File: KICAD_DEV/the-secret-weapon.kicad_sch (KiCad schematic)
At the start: 10 parts, among them J1 USB_C_Receptacle_USB2.0_14P, U1 STM32H757IITx, U2 TPS26750, U3 TPD4S480

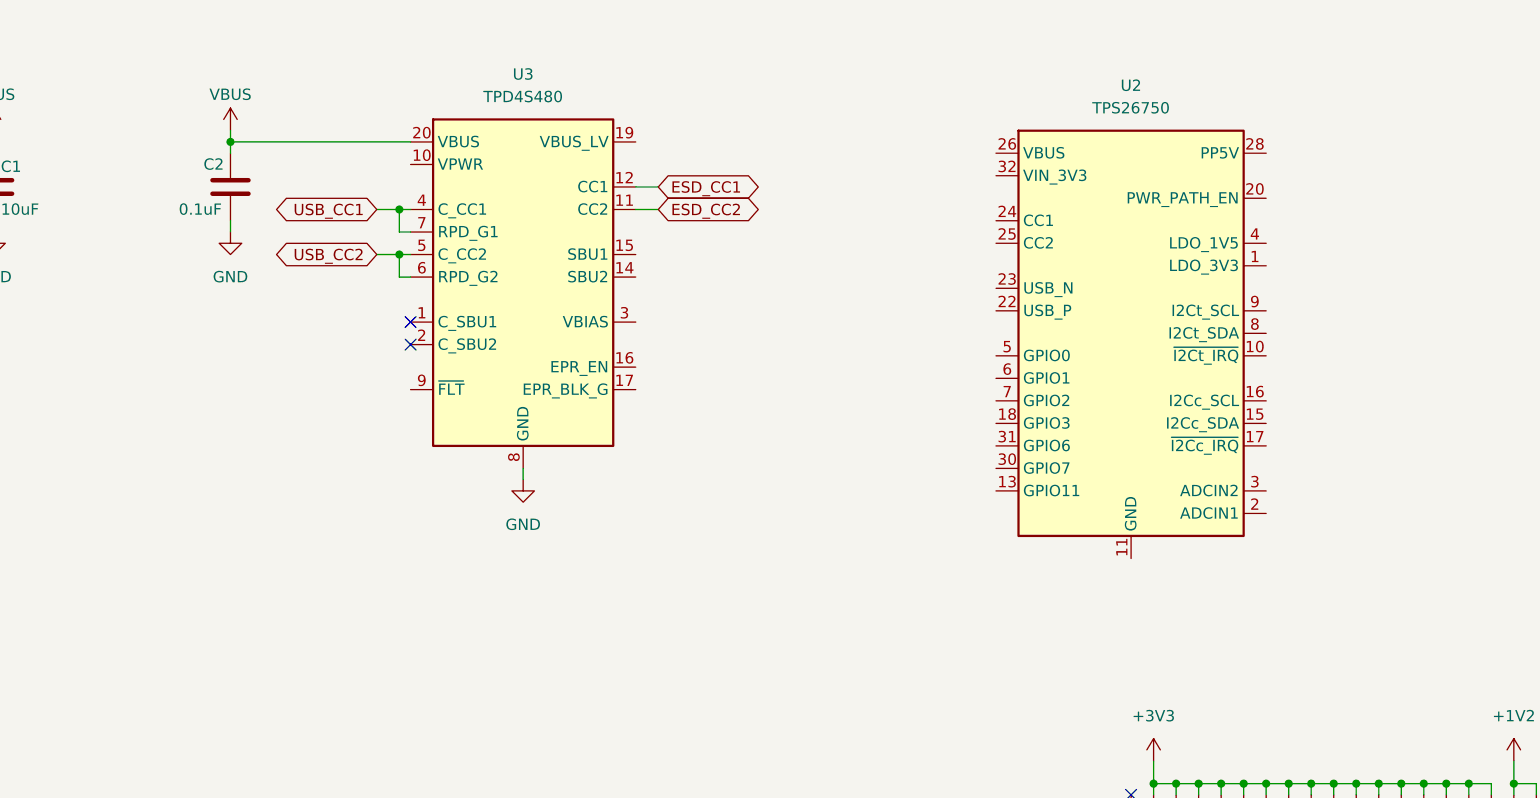
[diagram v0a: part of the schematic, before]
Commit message: finished wiring USB ESD protection
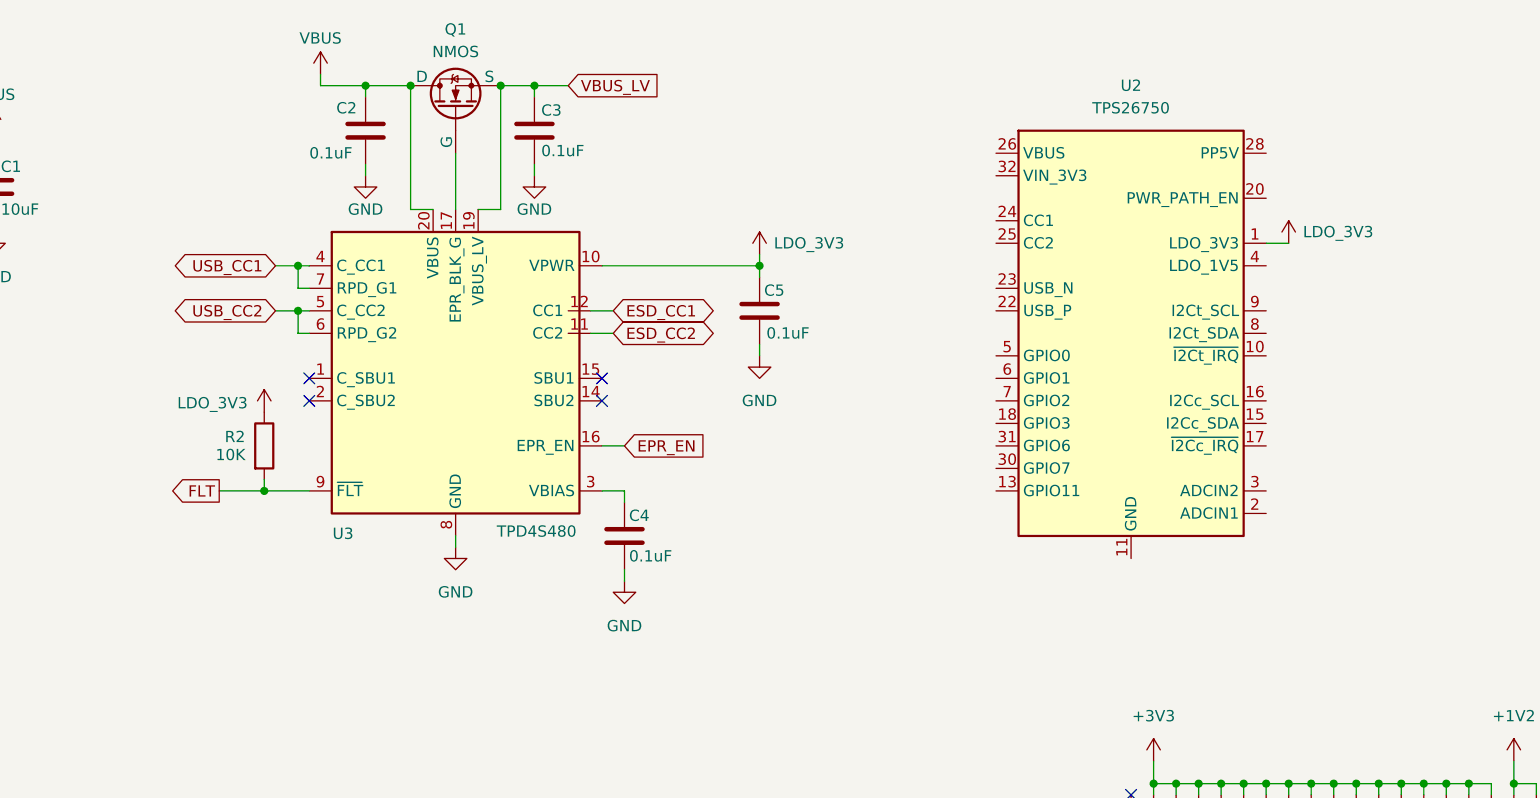
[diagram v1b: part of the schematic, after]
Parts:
- added C3, C4, C5: 0.1uF, symbol Device:C
- added Q1: NMOS, symbol Simulation_SPICE:NMOS
- added R2: 10K, symbol Device:R
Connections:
- net GND: now also C3.2, C4.2, C5.2; no longer U3.13 (GND), U3.16 (EPR_EN), U3.17 (EPR_BLK_G), U3.18 (GND), U3.21 (GND)
- net VBUS: now also Q1.1 (D)
- net LDO_3V3: now reaches U2.1 (LDO_3V3)
- net LDO_3V3: now also U3.10 (VPWR), C5.1, R2.1
- net EPR_EN: now reaches U3.16 (EPR_EN)
- net at U3.17 (EPR_BLK_G): now also Q1.2 (G)
- net VBUS_LV: now reaches U3.19 (VBUS_LV)
- net VBUS_LV: now also C3.1, Q1.3 (S)
- net at U3.3 (VBIAS): now also C4.1
- net FLT: now reaches U3.9 (~{FLT})
- net FLT: now also R2.2
- new net: U3.13 (GND), U3.16 (EPR_EN)
- new net: U3.17 (EPR_BLK_G), U3.18 (GND), U3.21 (GND)
- no-connect marks 3 -> 5
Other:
- moved on the sheet: U3

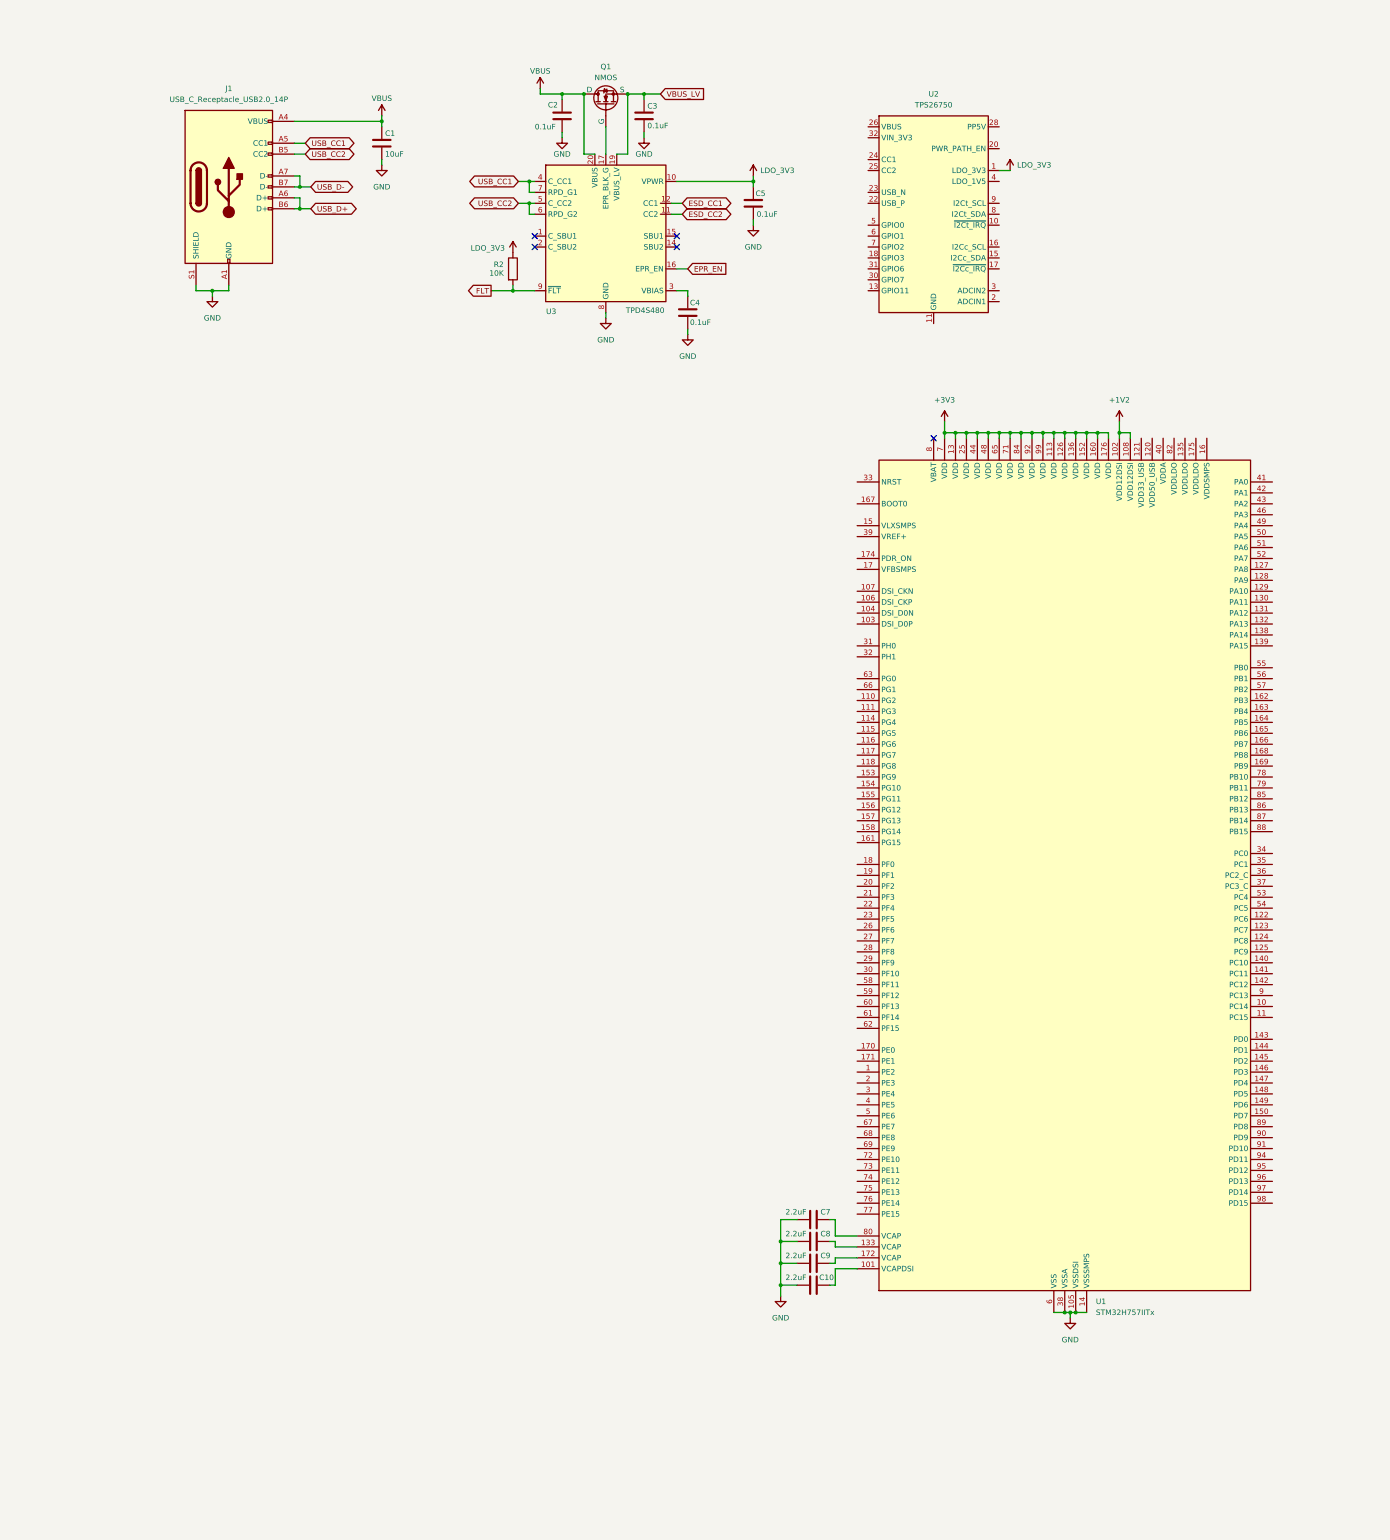
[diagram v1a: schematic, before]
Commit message: starting to wire my USB PD
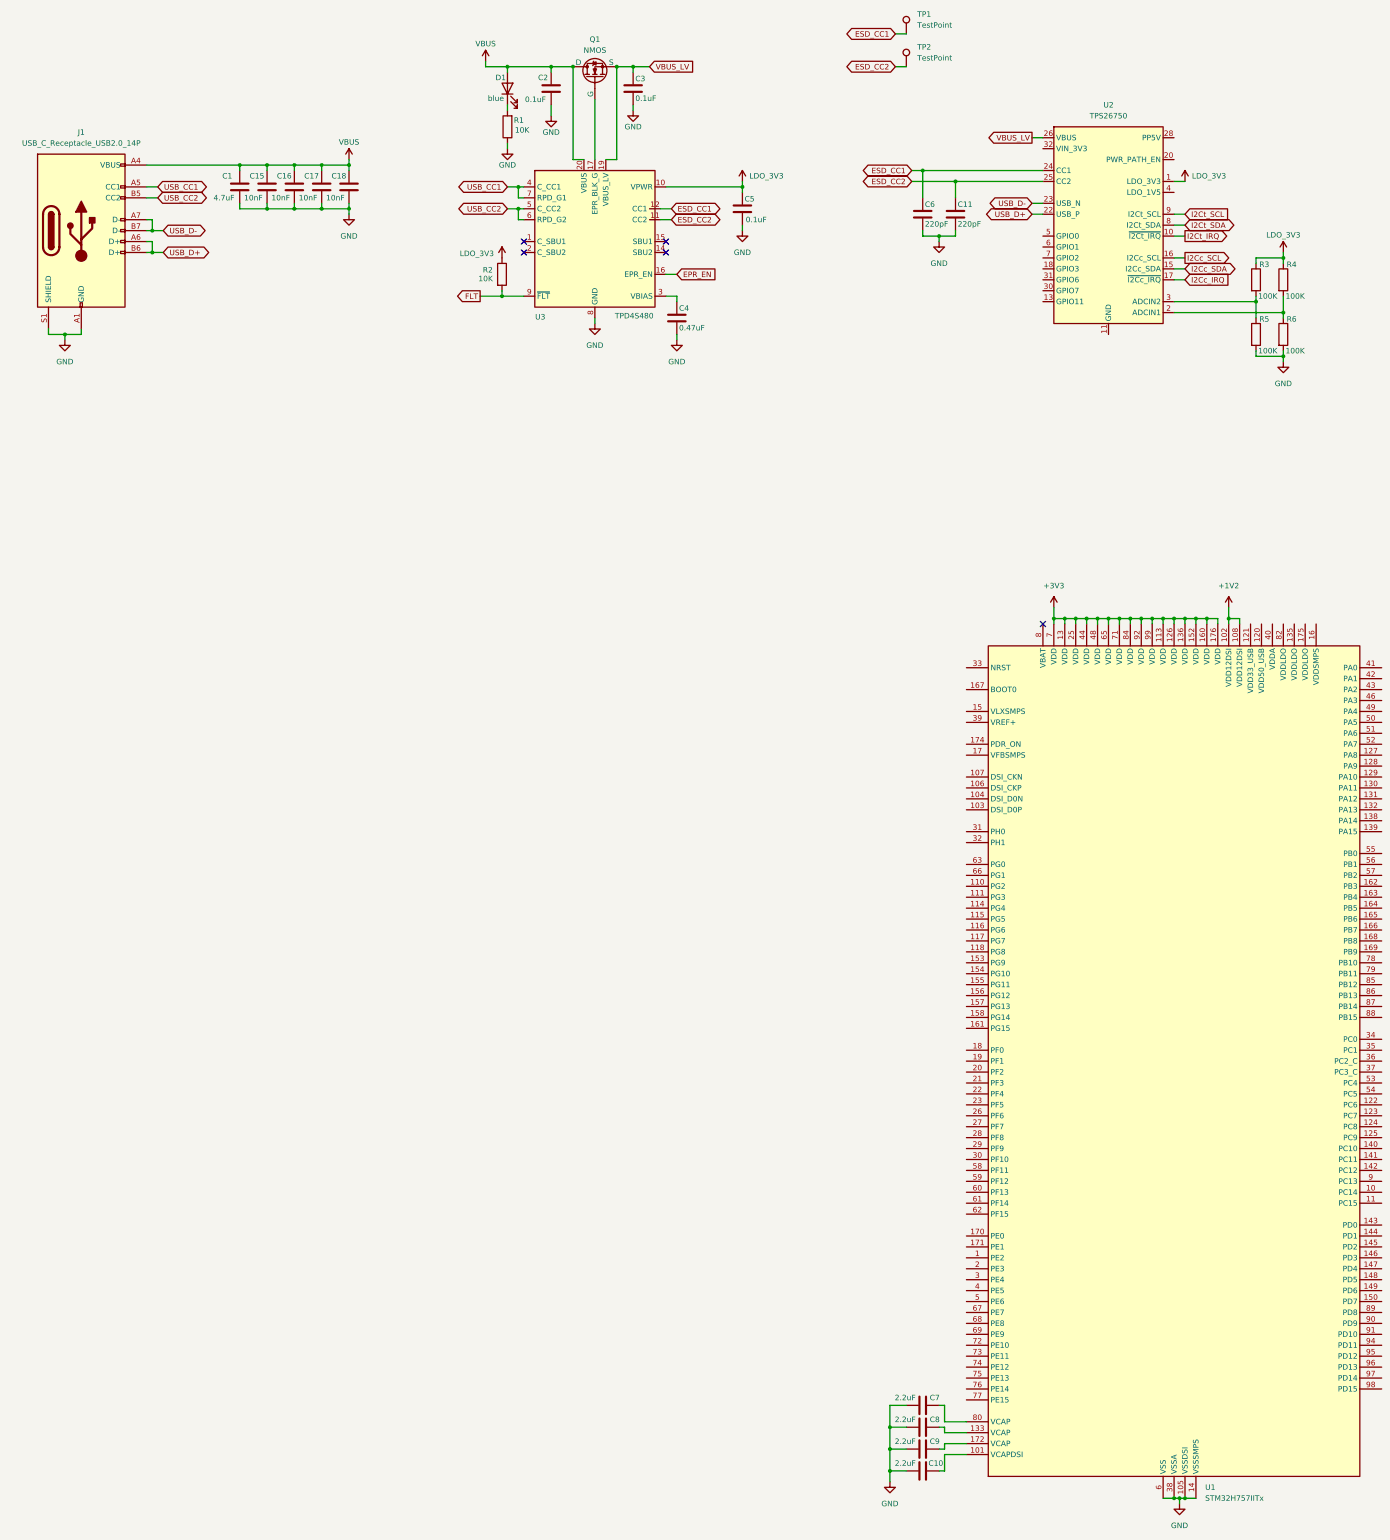
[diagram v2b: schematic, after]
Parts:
- added C11, C6: 220pF, symbol Device:C
- added C15, C16, C17, C18: 10nF, symbol Device:C
- added D1: blue, symbol Device:LED
- added R1: 10K, symbol Device:R
- added R3, R4, R5, R6: 100K, symbol Device:R
- added TP1, TP2: TestPoint, symbol Connector:TestPoint
- C1: value 10uF -> 4.7uF
- C4: value 0.1uF -> 0.47uF
- U2: footprint Package_DFN_QFN:Texas_RSN_WQFN-32-1EP_4x4mm_P0.4mm_EP2.8x2.8mm_ThermalVias -> Package_DFN_QFN:VQFN-32-1EP_4x4mm_P0.4mm_EP2.8x2.8mm_ThermalVias
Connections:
- net ESD_CC1: now also U2.24 (CC1), C6.1, TP1.1
- net ESD_CC2: now also U2.25 (CC2), C11.1, TP2.1
- net GND: now also C11.2, C15.2, C16.2, C17.2, C18.2, C6.2, R1.1, R5.2, R6.2
- net LDO_3V3: now also R3.1, R4.1
- net USB_D+: now also U2.22 (USB_P)
- net USB_D-: now also U2.23 (USB_N)
- net VBUS: now also C15.1, C16.1, C17.1, C18.1, D1.2 (A)
- net VBUS_LV: now also U2.26 (VBUS)
- net I2Ct_IRQ: now reaches U2.10 (~{I2Ct_IRQ})
- net I2Cc_SDA: now reaches U2.15 (I2Cc_SDA)
- net I2Cc_SCL: now reaches U2.16 (I2Cc_SCL)
- net I2Cc_IRQ: now reaches U2.17 (~{I2Cc_IRQ})
- net at U2.2 (ADCIN1): now also R4.2, R6.1
- net at U2.3 (ADCIN2): now also R3.2, R5.1
- net I2Ct_SDA: now reaches U2.8 (I2Ct_SDA)
- net I2Ct_SCL: now reaches U2.9 (I2Ct_SCL)
- new net: D1.1 (K), R1.2
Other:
- moved on the sheet: C10, C2, C3, C4, C5, C7, C8, C9, J1, Q1, R2, U1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

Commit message: more progress on USB PD
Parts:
- added C12, C13: 10uF, symbol Device:C
- added R10, R11, R7, R8: 2.2K, symbol Device:R
- added R12, R9: 10K, symbol Device:R
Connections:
- net GND: now also U2.11 (GND), U2.12 (GND), U2.14 (GND), U2.16 (I2Cc_SCL), U2.17 (~{I2Cc_IRQ}), U2.31 (GND), U2.34 (GND), U2.39 (GND), C12.2, C13.2
- net I2Cc_IRQ: now also R12.2
- net I2Cc_SCL: now also R10.2
- net I2Cc_SDA: now also R11.2
- net I2Ct_IRQ: now also R9.2
- net I2Ct_SCL: now also R7.2
- net I2Ct_SDA: now also R8.2
- net LDO_3V3: now also C12.1, R10.1, R11.1, R12.1, R7.1, R8.1, R9.1
- net ADCIN1: now reaches R4.2, R6.1
- net ADCIN1: now also U2.3 (ADCIN2); no longer U2.2 (ADCIN1)
- net ADCIN2: now reaches R3.2, R5.1
- net ADCIN2: now also U2.2 (ADCIN1); no longer U2.3 (ADCIN2)
- net LDO_1V5: now reaches U2.4 (LDO_1V5)
- net LDO_1V5: now also C13.1
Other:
- moved on the sheet: R4, R6

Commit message: almost done USB PD wiring (this is a lie)
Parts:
- removed C1: 4.7uF, symbol Device:C
- removed C11, C6: 220pF, symbol Device:C
- removed C12, C13: 10uF, symbol Device:C
- removed C15, C16, C17, C18: 10nF, symbol Device:C
- removed C2, C3, C5: 0.1uF, symbol Device:C
- removed C4: 0.47uF, symbol Device:C
- removed D1: blue, symbol Device:LED
- removed J1: USB_C_Receptacle_USB2.0_14P, symbol Connector:USB_C_Receptacle_USB2.0_14P
- removed Q1: NMOS, symbol Simulation_SPICE:NMOS
- removed R1, R12, R2, R9: 10K, symbol Device:R
- removed R10, R11, R7, R8: 2.2K, symbol Device:R
- removed R3, R4, R5, R6: 100K, symbol Device:R
- removed TP1, TP2: TestPoint, symbol Connector:TestPoint
- removed U2: TPS26750, Package_DFN_QFN:VQFN-32-1EP_4x4mm_P0.4mm_EP2.8x2.8mm_ThermalVias, symbol kai-library:TPS26750
- removed U3: TPD4S480, Package_DFN_QFN:WQFN-20-1EP_3x3mm_P0.4mm_EP1.7x1.7mm_ThermalVias, symbol kai-library:TPD4S480
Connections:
- no-connect marks 5 -> 1
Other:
- added sheet USB-C PD (USB-C-PD.kicad_sch)

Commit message: some school shenanigans
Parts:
- removed C10, C7, C8, C9: 2.2uF, symbol Device:C
- removed U1: STM32H757IITx, Package_QFP:LQFP-176_24x24mm_P0.5mm, symbol MCU_ST_STM32H7:STM32H757IITx
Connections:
- no-connect marks 1 -> 0
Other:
- added sheet Brain MCU (brain-mcu.kicad_sch)

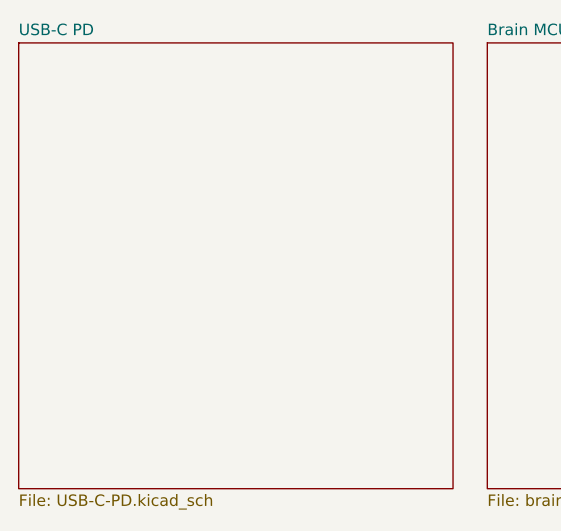
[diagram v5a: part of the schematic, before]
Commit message: working on the buck converter!
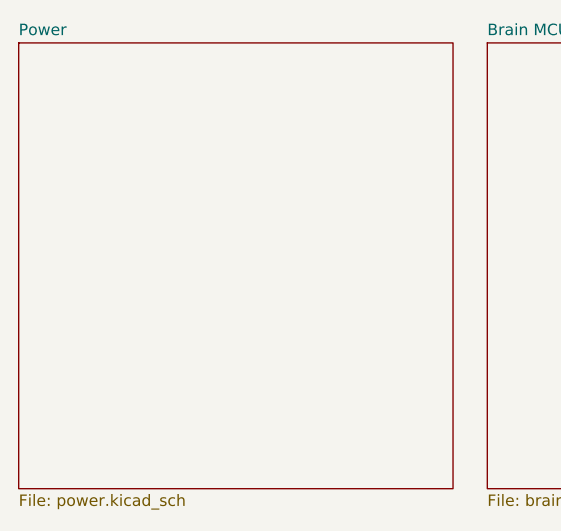
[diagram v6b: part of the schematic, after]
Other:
- sheet USB-C PD renamed Power
- sheet Power: file USB-C-PD.kicad_sch -> power.kicad_sch
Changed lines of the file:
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@@
 			(color 0 0 0 0.0000)
 		)
-		(property "Sheetname" "USB-C PD"
+		(property "Sheetname" "Power"
 			(at 17.78 17.0684 0)
 			(effects
@@
 			)
 		)
-		(property "Sheetfile" "USB-C-PD.kicad_sch"
+		(property "Sheetfile" "power.kicad_sch"
 			(at 17.78 67.8946 0)
 			(effects
